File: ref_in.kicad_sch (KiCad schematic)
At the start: 19 parts

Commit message: Schematic updated
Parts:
- C801, C802, C804, C805: renamed from C?; footprint (none) -> Capacitor_SMD:C_0805_2012Metric
- C803: renamed from C?; value 100n -> 100n/U2J; footprint (none) -> Capacitor_SMD:C_0805_2012Metric
- R801, R802, R803, R804: renamed from R?; footprint (none) -> Resistor_SMD:R_0805_2012Metric
- gave numbers to parts that had none: 6
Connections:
- net at C802.2, D802.2 (A), D803.1 (K)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: now also R803.1; no longer R803.2
- net at C803.2, R804.2: now also R803.2; no longer R803.1
- net +3.3VA renamed +3.3VD
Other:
- moved on the sheet: C803, C804, C805, R803, R804, U801C, U802C

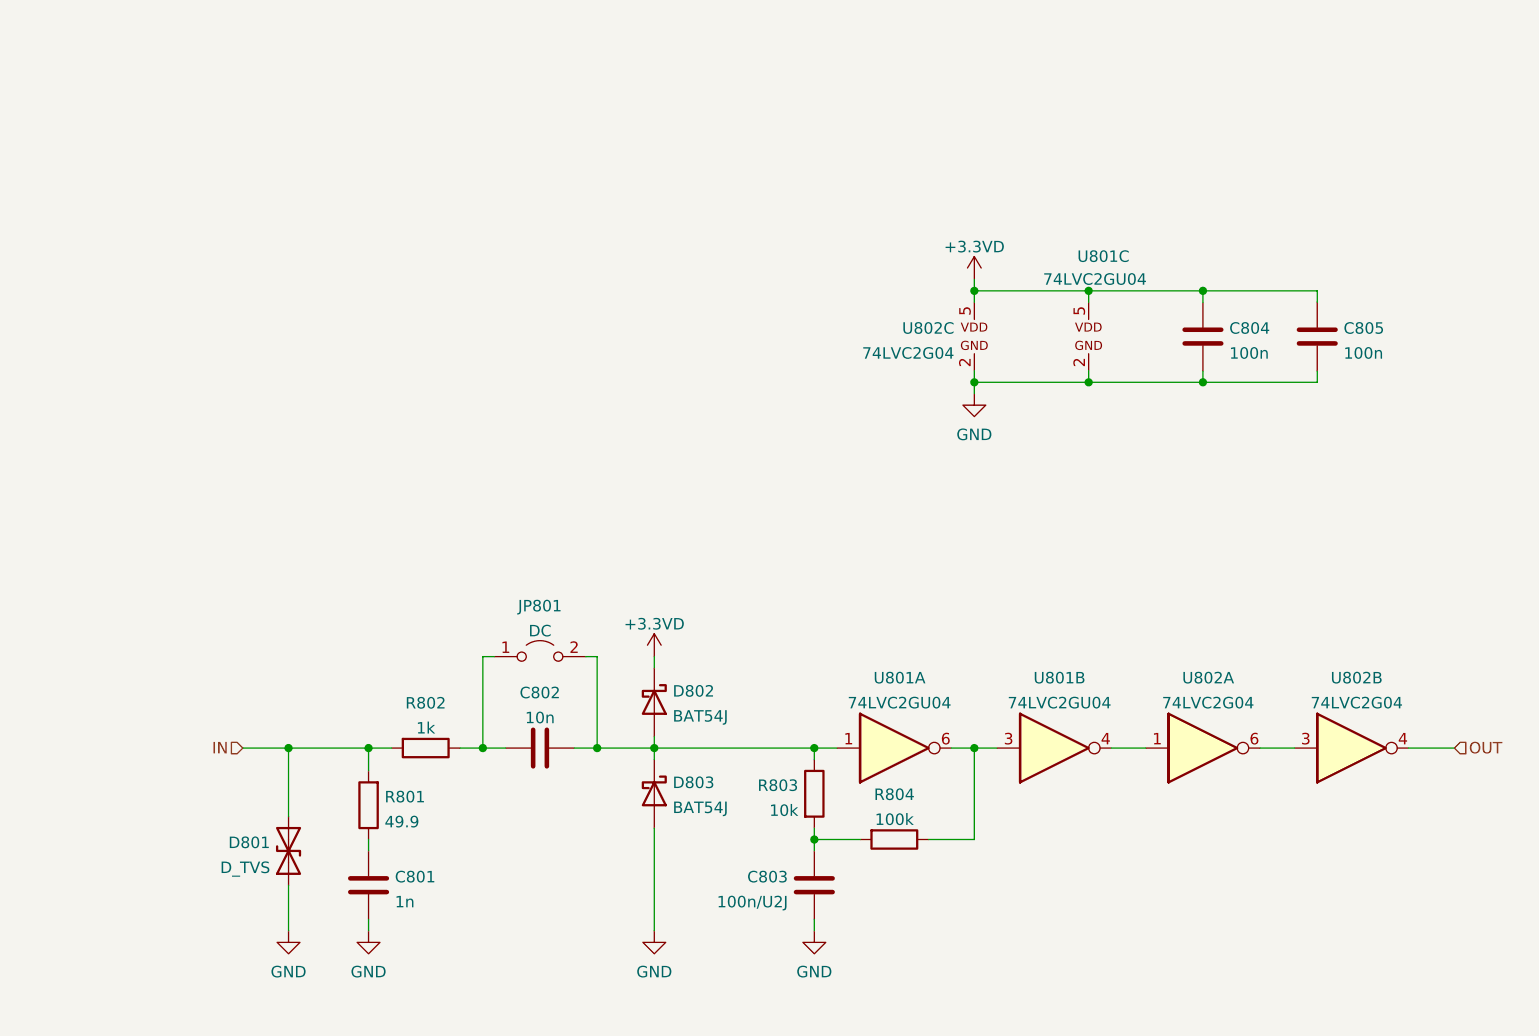
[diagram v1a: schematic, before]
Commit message: Schematic sketching done
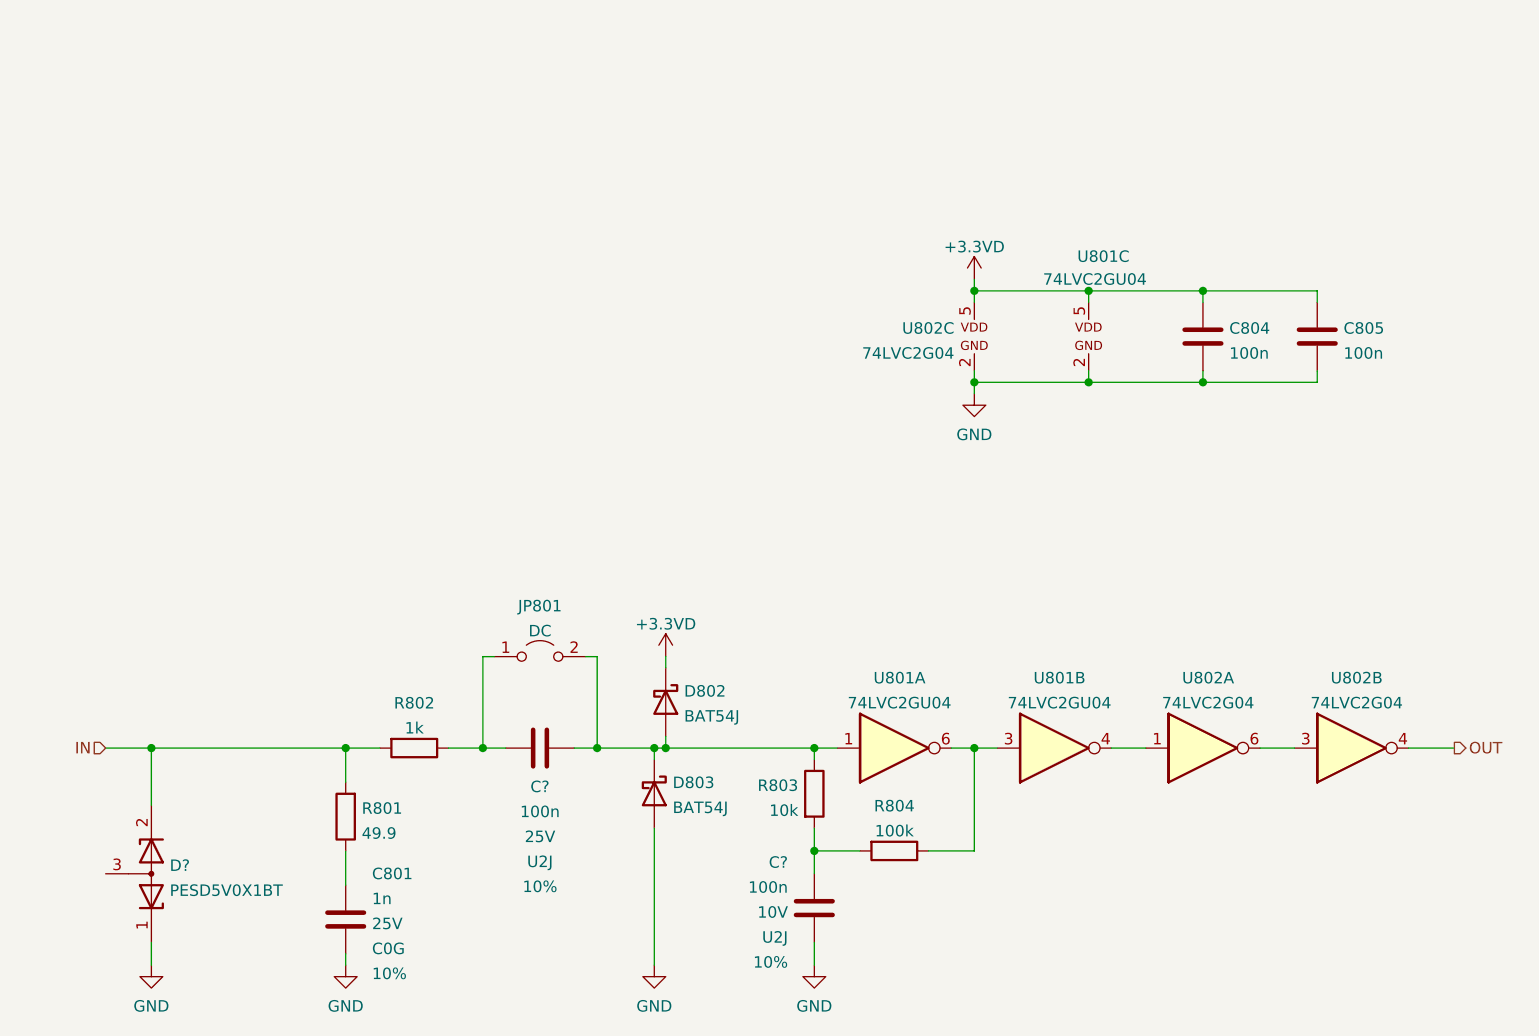
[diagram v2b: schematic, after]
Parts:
- removed C802: 10n, Capacitor_SMD:C_0805_2012Metric, symbol Device:C
- removed C803: 100n/U2J, Capacitor_SMD:C_0805_2012Metric, symbol Device:C
- removed D801: D_TVS, symbol Device:D_TVS
- added C? (x2): 100n, Capacitor_SMD:C_0805_2012Metric, symbol Device:C
- added D?: PESD5V0X1BT, Package_TO_SOT_SMD:SOT-23, symbol Device:D_Zener_Dual_CommonAnode_KKA
- C801: Spec1 (none) -> 25V; Spec2 (none) -> C0G; Tolerance (none) -> 10%
- R801, R802, R803, R804: Tolerance (none) -> 5%
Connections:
- net GND: now also C?.2, D?.1 (K)
- net IN: now also D?.2 (K)
- net at D802.2 (A), D803.1 (K), JP801.2 (B)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: now also C?.2
- net at R803.2, R804.2: now also C?.1
- net at JP801.1 (A), R802.1: now also C?.1
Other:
- moved on the sheet: C801, D802, R801, R802, R804

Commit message: Update schematic layout, separate into sheets
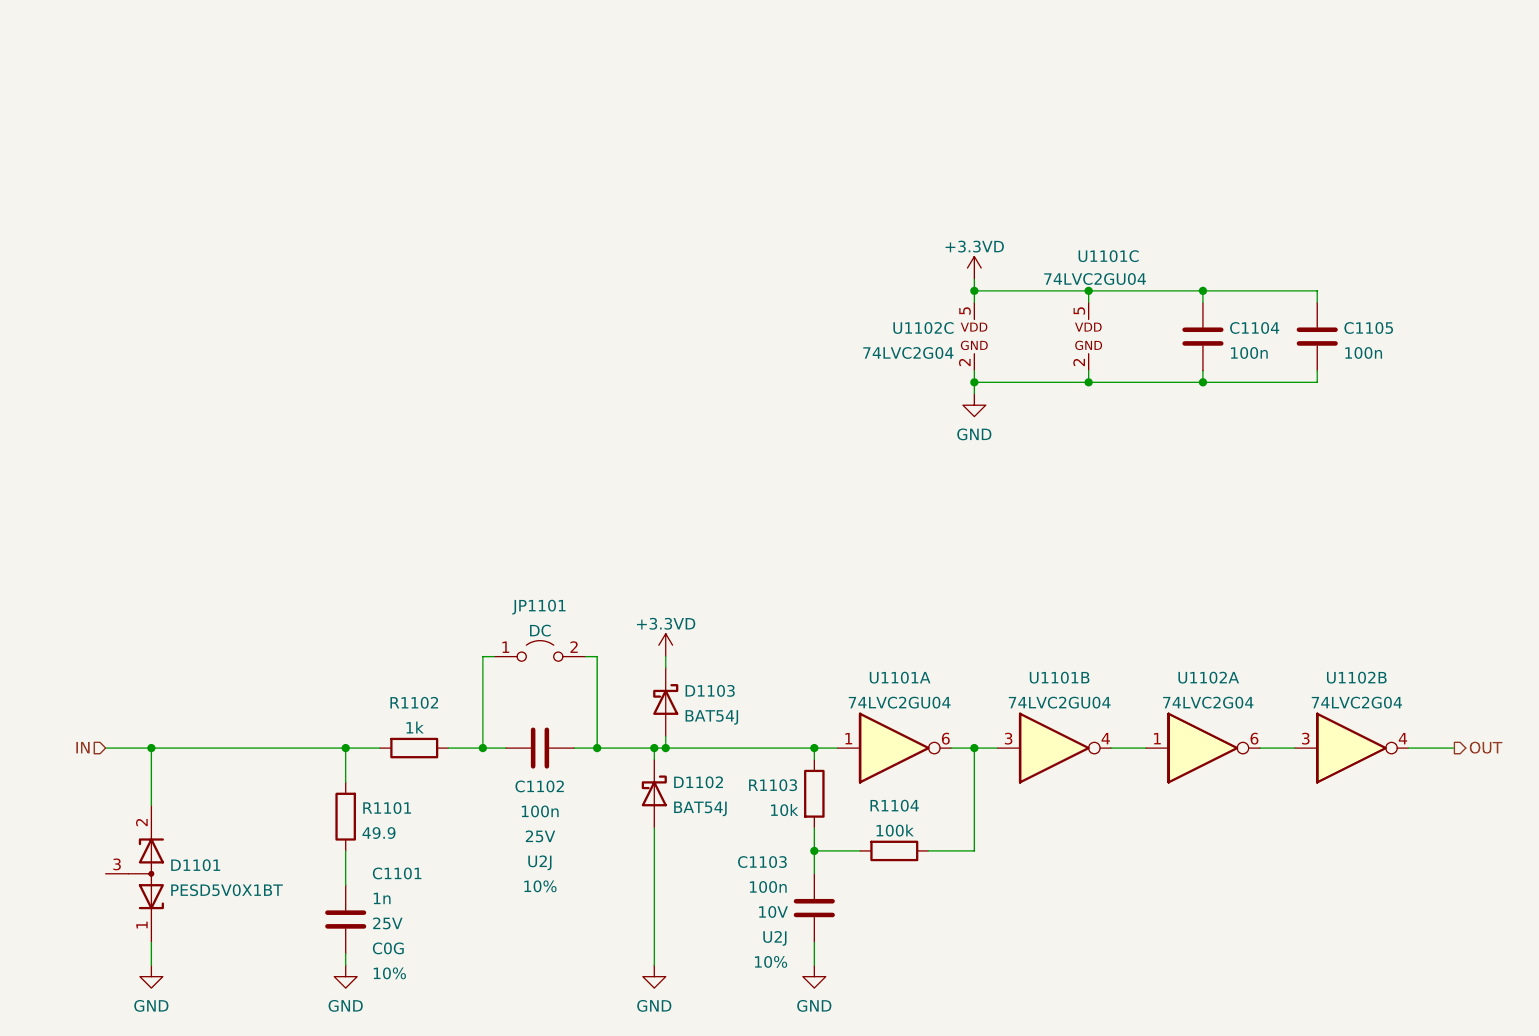
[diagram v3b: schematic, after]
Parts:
- gave numbers to parts that had none: 3
- renumbered C801 to C1101, C804 to C1104, C805 to C1105, D803 to D1102, D802 to D1103, JP801 to JP1101, R801 to R1101, R802 to R1102, R803 to R1103, R804 to R1104, U801 to U1101, U802 to U1102
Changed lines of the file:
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@@
   (symbol (lib_id "Diode:BAT54J") (at 130.81 96.52 270) (unit 1)
     (in_bom yes) (on_board yes) (fields_autoplaced)
-    (property "Reference" "D802" (id 0) (at 132.842 95.294 90)
+    (property "Reference" "D1103" (id 0) (at 132.842 95.294 90)
       (effects (font (size 1.27 1.27)) (justify left))
     )
@@
   (symbol (lib_id "symbols:74LVC2G04") (at 165.1 55.88 0) (unit 3)
     (in_bom yes) (on_board yes) (fields_autoplaced)
-    (property "Reference" "U802" (id 0) (at 162.8788 54.9715 0)
+    (property "Reference" "U1102" (id 0) (at 162.8788 54.9715 0)
       (effects (font (size 1.27 1.27)) (justify right))
     )
@@
   (symbol (lib_id "Device:D_Zener_Dual_CommonAnode_KKA") (at 73.66 115.57 270) (mirror x) (unit 1)
     (in_bom yes) (on_board yes) (fields_autoplaced)
-    (property "Reference" "D?" (id 0) (at 75.692 114.6615 90)
+    (property "Reference" "D1101" (id 0) (at 75.692 114.6615 90)
       (effects (font (size 1.27 1.27)) (justify left))
     )
@@
   (symbol (lib_id "Device:C") (at 116.84 101.6 90) (unit 1)
     (in_bom yes) (on_board yes) (fields_autoplaced)
-    (property "Reference" "C?" (id 0) (at 116.84 105.9085 90))
+    (property "Reference" "C1102" (id 0) (at 116.84 105.9085 90))
     (property "Value" "100n" (id 1) (at 116.84 108.6836 90))
     (property "Footprint" "Capacitor_SMD:C_0805_2012Metric" (id 2) (at 120.65 100.6348 0)
@@
   (symbol (lib_id "Device:C") (at 190.5 55.88 180) (unit 1)
     (in_bom yes) (on_board yes) (fields_autoplaced)
-    (property "Reference" "C804" (id 0) (at 193.421 54.9715 0)
+    (property "Reference" "C1104" (id 0) (at 193.421 54.9715 0)
       (effects (font (size 1.27 1.27)) (justify right))
     )
@@
   (symbol (lib_id "power:GND") (at 165.1 62.23 0) (unit 1)
     (in_bom yes) (on_board yes) (fields_autoplaced)
-    (property "Reference" "#PWR0807" (id 0) (at 165.1 68.58 0)
+    (property "Reference" "#PWR01107" (id 0) (at 165.1 68.58 0)
       (effects (font (size 1.27 1.27)) hide)
     )
@@
   (symbol (lib_id "Jumper:Jumper_2_Open") (at 116.84 91.44 0) (unit 1)
     (in_bom yes) (on_board yes) (fields_autoplaced)
-    (property "Reference" "JP801" (id 0) (at 116.84 85.8225 0))
+    (property "Reference" "JP1101" (id 0) (at 116.84 85.8225 0))
     (property "Value" "DC" (id 1) (at 116.84 88.5976 0))
     (property "Footprint" "" (id 2) (at 116.84 91.44 0)
@@
   (symbol (lib_id "power:GND") (at 73.66 125.73 0) (unit 1)
     (in_bom yes) (on_board yes) (fields_autoplaced)
-    (property "Reference" "#PWR0801" (id 0) (at 73.66 132.08 0)
+    (property "Reference" "#PWR01101" (id 0) (at 73.66 132.08 0)
       (effects (font (size 1.27 1.27)) hide)
     )
@@
   (symbol (lib_id "Device:R") (at 95.25 109.22 180) (unit 1)
     (in_bom yes) (on_board yes) (fields_autoplaced)
-    (property "Reference" "R801" (id 0) (at 97.028 108.3115 0)
+    (property "Reference" "R1101" (id 0) (at 97.028 108.3115 0)
       (effects (font (size 1.27 1.27)) (justify right))
     )
@@
   (symbol (lib_id "Device:R") (at 156.21 113.03 270) (unit 1)
     (in_bom yes) (on_board yes) (fields_autoplaced)
-    (property "Reference" "R804" (id 0) (at 156.21 108.0475 90))
+    (property "Reference" "R1104" (id 0) (at 156.21 108.0475 90))
     (property "Value" "100k" (id 1) (at 156.21 110.8226 90))
     (property "Footprint" "Resistor_SMD:R_0805_2012Metric" (id 2) (at 156.21 111.252 90)
@@
   (symbol (lib_id "Device:C") (at 147.32 119.38 0) (unit 1)
     (in_bom yes) (on_board yes) (fields_autoplaced)
-    (property "Reference" "C?" (id 0) (at 144.399 114.3088 0)
+    (property "Reference" "C1103" (id 0) (at 144.399 114.3088 0)
       (effects (font (size 1.27 1.27)) (justify right))
     )
@@
   (symbol (lib_id "symbols:74LVC2GU04") (at 172.72 101.6 0) (unit 2)
     (in_bom yes) (on_board yes) (fields_autoplaced)
-    (property "Reference" "U801" (id 0) (at 174.5615 93.8235 0))
+    (property "Reference" "U1101" (id 0) (at 174.5615 93.8235 0))
     (property "Value" "74LVC2GU04" (id 1) (at 174.5615 96.5986 0))
     (property "Footprint" "Package_TO_SOT_SMD:SOT-23-6" (id 2) (at 172.72 83.82 0)
@@
   (symbol (lib_id "power:GND") (at 129.54 125.73 0) (unit 1)
     (in_bom yes) (on_board yes) (fields_autoplaced)
-    (property "Reference" "#PWR0804" (id 0) (at 129.54 132.08 0)
+    (property "Reference" "#PWR01103" (id 0) (at 129.54 132.08 0)
       (effects (font (size 1.27 1.27)) hide)
     )
@@
   (symbol (lib_id "symbols:+3.3VD") (at 130.81 91.44 0) (unit 1)
     (in_bom yes) (on_board yes)
-    (property "Reference" "#PWR0803" (id 0) (at 130.81 95.25 0)
+    (property "Reference" "#PWR01104" (id 0) (at 130.81 95.25 0)
       (effects (font (size 1.27 1.27)) hide)
     )
@@
   (symbol (lib_id "symbols:74LVC2GU04") (at 177.8 55.88 0) (unit 3)
     (in_bom yes) (on_board yes)
-    (property "Reference" "U801" (id 0) (at 176.53 46.99 0)
+    (property "Reference" "U1101" (id 0) (at 176.53 46.99 0)
       (effects (font (size 1.27 1.27)) (justify left))
     )
@@
   (symbol (lib_id "Device:C") (at 95.25 120.65 0) (unit 1)
     (in_bom yes) (on_board yes) (fields_autoplaced)
-    (property "Reference" "C801" (id 0) (at 98.171 115.5788 0)
+    (property "Reference" "C1101" (id 0) (at 98.171 115.5788 0)
       (effects (font (size 1.27 1.27)) (justify left))
     )
@@
   (symbol (lib_id "symbols:74LVC2G04") (at 189.23 101.6 0) (unit 1)
     (in_bom yes) (on_board yes) (fields_autoplaced)
-    (property "Reference" "U802" (id 0) (at 191.0715 93.8235 0))
+    (property "Reference" "U1102" (id 0) (at 191.0715 93.8235 0))
     (property "Value" "74LVC2G04" (id 1) (at 191.0715 96.5986 0))
     (property "Footprint" "Package_TO_SOT_SMD:SOT-23-6" (id 2) (at 189.23 83.82 0)
@@
   (symbol (lib_id "power:GND") (at 147.32 125.73 0) (unit 1)
     (in_bom yes) (on_board yes) (fields_autoplaced)
-    (property "Reference" "#PWR0805" (id 0) (at 147.32 132.08 0)
+    (property "Reference" "#PWR01105" (id 0) (at 147.32 132.08 0)
       (effects (font (size 1.27 1.27)) hide)
     )
@@
     (pin "1")
   )
-  (symbol (lib_name "+3.3VD_1") (lib_id "symbols:+3.3VD") (at 165.1 49.53 0) (unit 1)
-    (in_bom yes) (on_board yes) (fields_autoplaced)
-    (property "Reference" "#PWR0806" (id 0) (at 165.1 53.34 0)
+  (symbol (lib_id "symbols:+3.3VD") (at 165.1 49.53 0) (unit 1)
+    (in_bom yes) (on_board yes) (fields_autoplaced)
+    (property "Reference" "#PWR01106" (id 0) (at 165.1 53.34 0)
       (effects (font (size 1.27 1.27)) hide)
     )
@@
   (symbol (lib_id "power:GND") (at 95.25 125.73 0) (unit 1)
     (in_bom yes) (on_board yes) (fields_autoplaced)
-    (property "Reference" "#PWR0802" (id 0) (at 95.25 132.08 0)
+    (property "Reference" "#PWR01102" (id 0) (at 95.25 132.08 0)
       (effects (font (size 1.27 1.27)) hide)
     )
@@
   (symbol (lib_id "Diode:BAT54J") (at 129.54 106.68 270) (unit 1)
     (in_bom yes) (on_board yes) (fields_autoplaced)
-    (property "Reference" "D803" (id 0) (at 131.572 105.454 90)
+    (property "Reference" "D1102" (id 0) (at 131.572 105.454 90)
       (effects (font (size 1.27 1.27)) (justify left))
     )
@@
   (symbol (lib_id "Device:C") (at 203.2 55.88 180) (unit 1)
     (in_bom yes) (on_board yes) (fields_autoplaced)
-    (property "Reference" "C805" (id 0) (at 206.121 54.9715 0)
+    (property "Reference" "C1105" (id 0) (at 206.121 54.9715 0)
       (effects (font (size 1.27 1.27)) (justify right))
     )
@@
   (symbol (lib_id "Device:R") (at 102.87 101.6 270) (unit 1)
     (in_bom yes) (on_board yes) (fields_autoplaced)
-    (property "Reference" "R802" (id 0) (at 102.87 96.6175 90))
+    (property "Reference" "R1102" (id 0) (at 102.87 96.6175 90))
     (property "Value" "1k" (id 1) (at 102.87 99.3926 90))
     (property "Footprint" "Resistor_SMD:R_0805_2012Metric" (id 2) (at 102.87 99.822 90)
@@
   (symbol (lib_id "symbols:74LVC2GU04") (at 154.94 101.6 0) (unit 1)
     (in_bom yes) (on_board yes) (fields_autoplaced)
-    (property "Reference" "U801" (id 0) (at 156.7815 93.8235 0))
+    (property "Reference" "U1101" (id 0) (at 156.7815 93.8235 0))
     (property "Value" "74LVC2GU04" (id 1) (at 156.7815 96.5986 0))
     (property "Footprint" "Package_TO_SOT_SMD:SOT-23-6" (id 2) (at 154.94 83.82 0)
@@
   (symbol (lib_id "symbols:74LVC2G04") (at 205.74 101.6 0) (unit 2)
     (in_bom yes) (on_board yes) (fields_autoplaced)
-    (property "Reference" "U802" (id 0) (at 207.5815 93.8235 0))
+    (property "Reference" "U1102" (id 0) (at 207.5815 93.8235 0))
     (property "Value" "74LVC2G04" (id 1) (at 207.5815 96.5986 0))
     (property "Footprint" "Package_TO_SOT_SMD:SOT-23-6" (id 2) (at 205.74 83.82 0)
@@
   (symbol (lib_id "Device:R") (at 147.32 106.68 0) (unit 1)
     (in_bom yes) (on_board yes) (fields_autoplaced)
-    (property "Reference" "R803" (id 0) (at 145.542 105.7715 0)
-      (effects (font (size 1.27 1.27)) (justify right))
-    )
+    (property "Reference" "R1103" (id 0) (at 145.542 105.7715 0)
+      (effects (font (size 1.27 1.27)) (justify right))
+    )

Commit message: Schematic update
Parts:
- C1102: footprint Capacitor_SMD:C_0805_2012Metric -> Capacitor_SMD:C_1206_3216Metric
- C1103: footprint Capacitor_SMD:C_0805_2012Metric -> Capacitor_SMD:C_1206_3216Metric; Spec1 10V -> 16V
- C1104, C1105: Spec1 (none) -> 16V; Spec2 (none) -> X5R; Tolerance (none) -> 20%
- JP1101: footprint (none) -> Connector_PinHeader_2.54mm:PinHeader_1x02_P2.54mm_Vertical
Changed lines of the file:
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@@
     (property "Reference" "C1102" (id 0) (at 116.84 105.9085 90))
     (property "Value" "100n" (id 1) (at 116.84 108.6836 90))
-    (property "Footprint" "Capacitor_SMD:C_0805_2012Metric" (id 2) (at 120.65 100.6348 0)
+    (property "Footprint" "Capacitor_SMD:C_1206_3216Metric" (id 2) (at 120.65 100.6348 0)
       (effects (font (size 1.27 1.27)) hide)
     )
@@
       (effects (font (size 1.27 1.27)) hide)
     )
+    (property "Spec1" "16V" (id 4) (at 190.5 55.88 0)
+      (effects (font (size 1.27 1.27)) hide)
+    )
+    (property "Spec2" "X5R" (id 5) (at 190.5 55.88 0)
+      (effects (font (size 1.27 1.27)) hide)
+    )
+    (property "Tolerance" "20%" (id 6) (at 190.5 55.88 0)
+      (effects (font (size 1.27 1.27)) hide)
+    )
     (pin "1")
     (pin "2")
@@
     (property "Reference" "JP1101" (id 0) (at 116.84 85.8225 0))
     (property "Value" "DC" (id 1) (at 116.84 88.5976 0))
-    (property "Footprint" "" (id 2) (at 116.84 91.44 0)
+    (property "Footprint" "Connector_PinHeader_2.54mm:PinHeader_1x02_P2.54mm_Vertical" (id 2) (at 116.84 91.44 0)
       (effects (font (size 1.27 1.27)) hide)
     )
@@
       (effects (font (size 1.27 1.27)) (justify right))
     )
-    (property "Footprint" "Capacitor_SMD:C_0805_2012Metric" (id 2) (at 148.2852 123.19 0)
+    (property "Footprint" "Capacitor_SMD:C_1206_3216Metric" (id 2) (at 148.2852 123.19 0)
       (effects (font (size 1.27 1.27)) hide)
     )
@@
       (effects (font (size 1.27 1.27)) hide)
     )
-    (property "Spec1" "10V" (id 5) (at 144.399 119.859 0)
+    (property "Spec1" "16V" (id 5) (at 144.399 119.859 0)
       (effects (font (size 1.27 1.27)) (justify right))
     )
@@
       (effects (font (size 1.27 1.27)) hide)
     )
+    (property "Spec1" "16V" (id 4) (at 203.2 55.88 0)
+      (effects (font (size 1.27 1.27)) hide)
+    )
+    (property "Spec2" "X5R" (id 5) (at 203.2 55.88 0)
+      (effects (font (size 1.27 1.27)) hide)
+    )
+    (property "Tolerance" "20%" (id 6) (at 203.2 55.88 0)
+      (effects (font (size 1.27 1.27)) hide)
+    )
